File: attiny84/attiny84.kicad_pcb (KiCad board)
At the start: 2 copper layers, 160 x 100 mm, 29 parts, among them J1 DIN41612_02x16_AB, J2 Banana Socket, J3 Banana Socket, J4 Banana Socket, J5 Banana Socket, SW1 SW_DIP_x08, U1 74151, U2 ATtiny84A-P, U3 L298HN

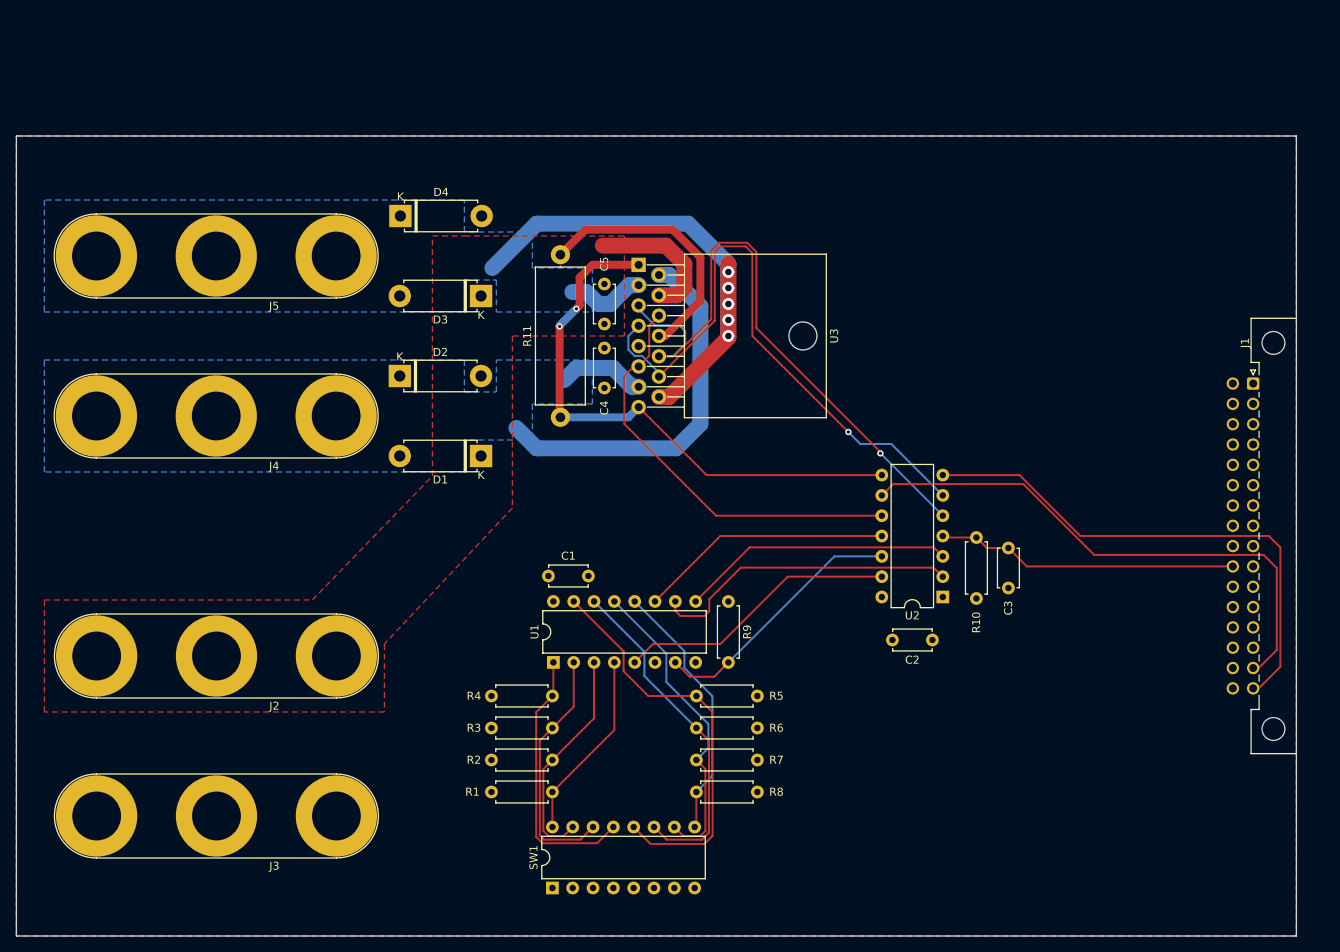
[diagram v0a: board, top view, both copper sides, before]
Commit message: Designed PCB for rev 0.3
The PCB has been designed for rev 0.3 of the circuit.

Signed-off-by: Matthew Nickson <mnickson@sidingsmedia.com>
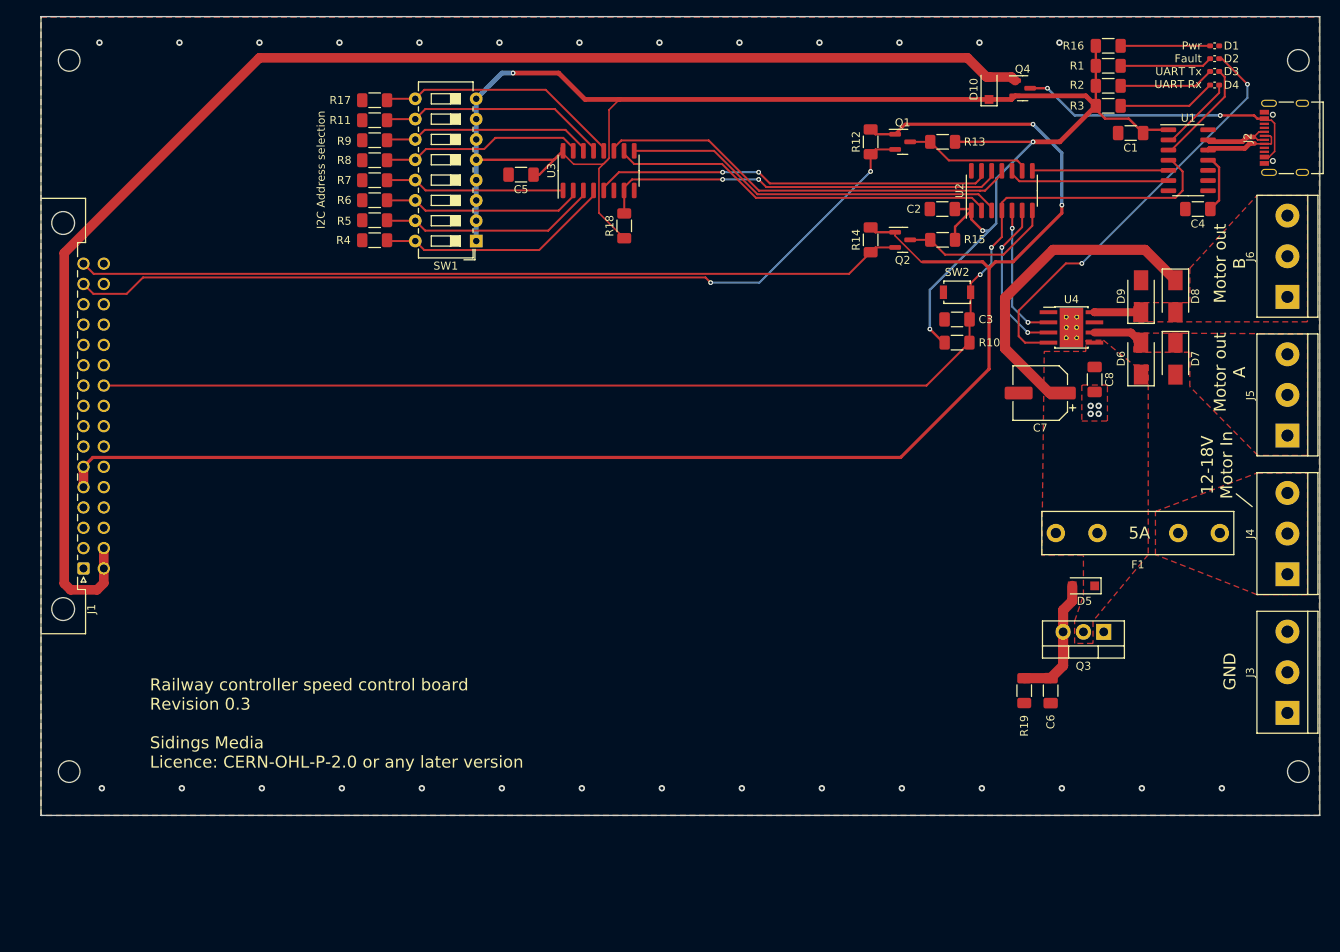
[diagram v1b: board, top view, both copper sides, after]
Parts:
- added C6: 47n, Capacitor_SMD:C_1206_3216Metric_Pad1.33x1.80mm_HandSolder, F.Cu at (181.3, 129.3)
- added C7: 47u, Capacitor_SMD:CP_Elec_6.3x5.7, F.Cu at (180.0, 92.1)
- added C8: 0.1uF, Capacitor_SMD:C_1206_3216Metric_Pad1.33x1.80mm_HandSolder, F.Cu at (186.8, 90.4)
- added D10: MBR1020VL, Diode_SMD:D_SOD-123F, F.Cu at (173.6, 54.0)
- added D5: 18V, Diode_SMD:D_SOD-123F, F.Cu at (185.4, 116.2)
- added D6: US1M, Diode_SMD:D_SMA, F.Cu at (192.6, 87.8)
- added D7: US1M, Diode_SMD:D_SMA, F.Cu at (196.9, 87.8)
- added D8: US1M, Diode_SMD:D_SMA, F.Cu at (196.9, 80.0)
- added D9: US1M, Diode_SMD:D_SMA, F.Cu at (192.6, 80.0)
- added F1: 5A, Fuse:Fuseholder_Littelfuse_445_030_series_5x20mm, F.Cu at (202.4, 109.6)
- added J6: Screw_Terminal_01x03, TerminalBlock:TerminalBlock_bornier-3_P5.08mm, F.Cu at (210.9, 80.1)
- added MK1: Mounting_Hole_PAD, Mounting_Holes:MountingHole_2.7mm, F.Cu at (58.6, 50.5)
- added MK2: Mounting_Hole_PAD, Mounting_Holes:MountingHole_2.7mm, F.Cu at (212.2, 50.5)
- added MK3: Mounting_Hole_PAD, Mounting_Holes:MountingHole_2.7mm, F.Cu at (58.6, 139.4)
- added MK4: Mounting_Hole_PAD, Mounting_Holes:MountingHole_2.7mm, F.Cu at (212.2, 139.4)
- added Q1: BSS138, Package_TO_SOT_SMD:SOT-23, F.Cu at (162.8, 60.7)
- added Q2: BSS138, Package_TO_SOT_SMD:SOT-23, F.Cu at (162.8, 73.0)
- added Q3: BT138-800, Package_TO_SOT_THT:TO-220-3_Vertical, F.Cu at (187.9, 122.0)
- added Q4: DMG2305UX, Package_TO_SOT_SMD:SOT-23, F.Cu at (177.8, 54.0)
- added R12: 10K, Resistor_SMD:R_1206_3216Metric_Pad1.30x1.75mm_HandSolder, F.Cu at (158.8, 60.7)
- added R13: 10K, Resistor_SMD:R_1206_3216Metric_Pad1.30x1.75mm_HandSolder, F.Cu at (167.8, 60.7)
- added R14: 10K, Resistor_SMD:R_1206_3216Metric_Pad1.30x1.75mm_HandSolder, F.Cu at (158.8, 73.0)
- added R15: 10K, Resistor_SMD:R_1206_3216Metric_Pad1.30x1.75mm_HandSolder, F.Cu at (167.8, 73.0)
- added R16: 330R, Resistor_SMD:R_1206_3216Metric_Pad1.30x1.75mm_HandSolder, F.Cu at (188.5, 48.7)
- added R17: 1K, Resistor_SMD:R_1206_3216Metric_Pad1.30x1.75mm_HandSolder, F.Cu at (96.8, 55.5)
- added R18: 1K, Resistor_SMD:R_1206_3216Metric_Pad1.30x1.75mm_HandSolder, F.Cu at (128.0, 71.2)
- added R19: 1K, Resistor_SMD:R_1206_3216Metric_Pad1.30x1.75mm_HandSolder, F.Cu at (178.0, 129.3)
- added SW2: SW_Push, Button_Switch_SMD:SW_SPST_B3U-1000P, F.Cu at (169.6, 79.5)
- added U4: DRV8872DDA, Package_SO:Texas_HTSOP-8-1EP_3.9x4.9mm_P1.27mm_EP2.95x4.9mm_Mask2.4x3.1mm_ThermalVias, F.Cu at (183.9, 83.9)
- C1: value 0.1uF -> 0.1u; footprint Capacitor_THT:C_Disc_D4.7mm_W2.5mm_P5.00mm -> Capacitor_SMD:C_1206_3216Metric_Pad1.33x1.80mm_HandSolder
- C2, C3, C5: footprint Capacitor_THT:C_Disc_D4.7mm_W2.5mm_P5.00mm -> Capacitor_SMD:C_1206_3216Metric_Pad1.33x1.80mm_HandSolder
- C4: value 0.1uF -> 1uF; footprint Capacitor_THT:C_Disc_D4.7mm_W2.5mm_P5.00mm -> Capacitor_SMD:C_1206_3216Metric_Pad1.33x1.80mm_HandSolder
- D1, D2, D3, D4: value D -> LED; footprint Diode_THT:D_5W_P10.16mm_Horizontal -> Capacitor_SMD:C_0402_1005Metric_Pad0.74x0.62mm_HandSolder
- J2: value Banana Socket -> USB_C_Receptacle_USB2.0; footprint Connector:Banana_Jack_3Pin -> Connector_USB:USB_C_Receptacle_Palconn_UTC16-G
- J3, J4, J5: value Banana Socket -> Screw_Terminal_01x03; footprint Connector:Banana_Jack_3Pin -> TerminalBlock:TerminalBlock_bornier-3_P5.08mm
- R1, R2, R3: value 1K -> 330R; footprint Resistor_THT:R_Axial_DIN0207_L6.3mm_D2.5mm_P7.62mm_Horizontal -> Resistor_SMD:R_1206_3216Metric_Pad1.30x1.75mm_HandSolder
- R10, R4, R5, R6, R7, R8, R9: footprint Resistor_THT:R_Axial_DIN0207_L6.3mm_D2.5mm_P7.62mm_Horizontal -> Resistor_SMD:R_1206_3216Metric_Pad1.30x1.75mm_HandSolder
- R11: value 0.5R -> 1K; footprint Resistor_THT:R_Axial_DIN0617_L17.0mm_D6.0mm_P20.32mm_Horizontal -> Resistor_SMD:R_1206_3216Metric_Pad1.30x1.75mm_HandSolder
- SW1: footprint Package_DIP:DIP-16_W7.62mm -> Button_Switch_THT:SW_DIP_SPSTx08_Slide_6.7x21.88mm_W7.62mm_P2.54mm_LowProfile
- U1: value 74151 -> MCP2221AxSL; footprint Package_DIP:DIP-16_W7.62mm -> Package_SO:SOIC-14_3.9x8.7mm_P1.27mm
- U2: footprint Package_DIP:DIP-14_W7.62mm -> Package_SO:SOIC-14_3.9x8.7mm_P1.27mm
- U3: value L298HN -> 74151; footprint Package_TO_SOT_THT:TO-220-15_P2.54x2.54mm_StaggerOdd_Lead5.84mm_TabDown -> Package_SO:SOIC-16_3.9x9.9mm_P1.27mm
- moved J1 148.0 mm to (60.4, 114.1), turned to 90 degrees
- moved J2 135.1 mm to (210.5, 60.2), turned to 90 degrees
- moved J5 121.0 mm to (210.9, 97.4), turned to 90 degrees
- moved J4 120.5 mm to (210.9, 114.8), turned to 90 degrees
- moved J3 119.6 mm to (210.9, 132.1), turned to 90 degrees
- moved R1 114.3 mm to (188.5, 51.2), turned to 0 degrees
- moved D2 109.3 mm to (201.8, 50.3), turned to 180 degrees
- moved R2 109.2 mm to (188.5, 53.7), turned to 0 degrees
- moved D1 105.1 mm to (201.8, 48.7)
- moved R3 104.3 mm to (188.5, 56.2), turned to 0 degrees
- moved D4 103.1 mm to (201.8, 53.6), turned to 180 degrees
- moved U1 101.2 mm to (198.5, 63.0), turned to 0 degrees
- moved D3 95.9 mm to (201.8, 51.9)
- moved C1 91.4 mm to (191.3, 59.6), turned to 180 degrees
- moved R8 88.6 mm to (96.8, 63.0), turned to 180 degrees
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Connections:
- C4 pad 1: +5V -> Net-(C4-Pad1)
- C5 pad 1: Net-(C5-Pad1) -> +5V
- D1 pad 1: Net-(C5-Pad1) -> GND
- D2 pad 1: Net-(D1-Pad2) -> /~{FAULT}
- D2 pad 2: GND -> Net-(D2-Pad2)
- D3 pad 1: Net-(C5-Pad1) -> /~{LED_UART_Tx}
- D4 pad 1: Net-(D3-Pad2) -> /~{LED_UART_Rx}
- D4 pad 2: GND -> Net-(D4-Pad2)
- J1 pad a15: /I2C_SCL -> Net-(J1-Pada15)
- J1 pad a16: /I2C_SDA -> Net-(J1-Pada16)
- J1 pad a5: unconnected-(J1-Pada5) -> +3V3
- J1 pad a6: unconnected-(J1-Pada6) -> +3V3
- J1 pad b1: +5V -> Net-(D10-Pad2)
- J1 pad b2: +5V -> Net-(D10-Pad2)
- J4 pad 1: Net-(D1-Pad2) -> Net-(F1-Pad1)
- J4 pad 2: Net-(D1-Pad2) -> Net-(F1-Pad1)
- J4 pad 3: Net-(D1-Pad2) -> Net-(F1-Pad1)
- J5 pad 1: Net-(D3-Pad2) -> Net-(D6-Pad2)
- J5 pad 2: Net-(D3-Pad2) -> Net-(D6-Pad2)
- J5 pad 3: Net-(D3-Pad2) -> Net-(D6-Pad2)
- R1 pad 1: Net-(R1-Pad1) -> +5V
- R1 pad 2: GND -> Net-(D2-Pad2)
- R11 pad 1: /L298_SENSE -> Net-(R11-Pad1)
- R2 pad 1: Net-(R2-Pad1) -> +5V
- R2 pad 2: GND -> Net-(D3-Pad2)
- R3 pad 1: Net-(R3-Pad1) -> +5V
- R3 pad 2: GND -> Net-(D4-Pad2)
- R9 pad 1: +5V -> Net-(R9-Pad1)
- R9 pad 2: /~{MUX_INPUT_EN} -> GND
- SW1 pad 10: Net-(R7-Pad1) -> Net-(R11-Pad1)
- SW1 pad 11: Net-(R6-Pad1) -> Net-(R9-Pad1)
- SW1 pad 12: Net-(R5-Pad1) -> Net-(R8-Pad1)
- SW1 pad 13: Net-(R4-Pad1) -> Net-(R7-Pad1)
- SW1 pad 14: Net-(R3-Pad1) -> Net-(R6-Pad1)
- SW1 pad 15: Net-(R2-Pad1) -> Net-(R5-Pad1)
- SW1 pad 16: Net-(R1-Pad1) -> Net-(R4-Pad1)
- SW1 pad 9: Net-(R8-Pad1) -> Net-(R17-Pad1)
- U1 pad 1: Net-(R4-Pad1) -> +5V
- U1 pad 10: /MUX_S1 -> unconnected-(U1-Pad10)
- U1 pad 11: /MUX_S0 -> Net-(C4-Pad1)
- U1 pad 12: Net-(R8-Pad1) -> /USB_D-
- U1 pad 13: Net-(R7-Pad1) -> /USB_D+
- U1 pad 14: Net-(R6-Pad1) -> GND
- U1 pad 2: Net-(R3-Pad1) -> /~{LED_UART_Rx}
- U1 pad 3: Net-(R2-Pad1) -> /~{LED_UART_Tx}
- U1 pad 4: Net-(R1-Pad1) -> /~{RESET}
- U1 pad 5: /MUX_OUT -> /UART_Tx
- U1 pad 6: unconnected-(U1-Pad6) -> /UART_Rx
- U1 pad 7: /~{MUX_INPUT_EN} -> unconnected-(U1-Pad7)
- U1 pad 8: GND -> unconnected-(U1-Pad8)
- U1 pad 9: /MUX_S2 -> unconnected-(U1-Pad9)
- U2 pad 10: /L298_EN -> /UART_Rx
- U2 pad 11: /MUX_S0 -> /I2C Address Selection/S0
- U2 pad 12: /~{MUX_INPUT_EN} -> /I2C Address Selection/~{INPUT_EN}
- U2 pad 13: /MUX_OUT -> /I2C Address Selection/OUT
- U2 pad 2: /MUX_S1 -> /I2C Address Selection/S1
- U2 pad 3: /MUX_S2 -> /I2C Address Selection/S2
- U2 pad 5: /L298_IN1 -> /Motor Driver/IN2
- U2 pad 6: /L298_IN2 -> /Motor Driver/IN1
- U2 pad 8: /L298_SENSE -> /UART_Tx
- U3 pad 1: /L298_SENSE -> Net-(R7-Pad1)
- U3 pad 10: /L298_IN1 -> /I2C Address Selection/S1
- U3 pad 11: /L298_EN -> /I2C Address Selection/S0
- U3 pad 12: /L298_IN2 -> Net-(R17-Pad1)
- U3 pad 13: Net-(D1-Pad2) -> Net-(R11-Pad1)
- U3 pad 14: Net-(D3-Pad2) -> Net-(R9-Pad1)
- U3 pad 15: /L298_SENSE -> Net-(R8-Pad1)
- U3 pad 2: Net-(D1-Pad2) -> Net-(R6-Pad1)
- U3 pad 3: Net-(D3-Pad2) -> Net-(R5-Pad1)
- U3 pad 4: Net-(C5-Pad1) -> Net-(R4-Pad1)
- U3 pad 5: /L298_IN1 -> /I2C Address Selection/OUT
- U3 pad 6: /L298_EN -> unconnected-(U3-Pad6)
- U3 pad 7: /L298_IN2 -> /I2C Address Selection/~{INPUT_EN}
- U3 pad 9: +5V -> /I2C Address Selection/S2
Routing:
- net +5V: track 0.00 -> 224.9 mm, vias 0 -> 4
- net +3V3: track 0.00 -> 196.2 mm, vias 0 -> 2
- net Net-(D10-Pad2): track 0.00 -> 181.4 mm
- net /~{RESET}: track 38.5 -> 157.6 mm, vias 0 -> 2
- net Net-(J1-Pada15): track 0.00 -> 111.2 mm, vias 0 -> 2
- net Net-(J1-Pada16): track 0.00 -> 103.4 mm
- net /L298_IN1: track 79.1 -> 0.00 mm, vias 1 -> 0
- net /L298_IN2: track 75.2 -> 0.00 mm, vias 1 -> 0
- net /L298_SENSE: track 70.8 -> 0.00 mm, vias 2 -> 0
- net Net-(D3-Pad2): track 73.9 -> 11.9 mm, vias 5 -> 0
- net /~{FAULT}: track 0.00 -> 53.4 mm, vias 0 -> 2
- net /I2C Address Selection/S0: track 0.00 -> 53.1 mm
- net /L298_EN: track 52.6 -> 0.00 mm
- net /I2C_SCL: track 67.7 -> 15.9 mm
- net /I2C Address Selection/~{INPUT_EN}: track 0.00 -> 51.3 mm, vias 0 -> 2
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- added copper zone on F.Cu, net GND
- added copper zone on F.Cu, net Net-(D6-Pad2)
- added copper zone on F.Cu, net Net-(D8-Pad2)
- added copper zone on F.Cu, net Net-(F1-Pad1)
- added copper zone on F.Cu, net VM
- removed copper zone on F.Cu, net +5V
- removed copper zone on F.Cu, net Net-(C5-Pad1)
- removed copper zone on B.Cu, net Net-(D1-Pad2)
- removed copper zone on B.Cu, net Net-(D3-Pad2)
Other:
- board size 160 x 100 mm -> 159.9 x 99.9 mm
- board text added: "12-18V Motor In"
- board text added: "5A"
- board text added: "GND"
- board text added: "I2C Address selection"
- board text added: "Motor out A"
- board text added: "Motor out B"
- board text added: "Pwr Fault UART Tx UART Rx"
- board text added: "Railway controller speed control board Revision 0.3 Sidings Media Licence: CERN-OHL-P-2.0 or any later version"
